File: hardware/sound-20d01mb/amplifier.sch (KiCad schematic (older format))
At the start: 0 parts

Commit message: Added TPA3122D2
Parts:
- added U?: TPA3122D2, Package_DIP:DIP-20_W7.62mm, symbol sound-20d01_Library:TPA3122D2
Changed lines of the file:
@@
 Comment4 ""
 $EndDescr
+$Comp
+L sound-20d01_Library:TPA3122D2 U?
+U 1 1 60DE3B7A
+P 5500 3500
+F 0 "U?" H 5500 4217 50  0000 C CNN
+F 1 "TPA3122D2" H 5500 4126 50  0000 C CNN
+F 2 "Package_DIP:DIP-20_W7.62mm" H 5500 2900 50  0001 C CNN
+F 3 "https://www.ti.com/lit/ds/symlink/tpa3122d2.pdf" H 5500 2800 50  0001 C CNN
+	1    5500 3500
+	1    0    0    -1
+$EndComp
 $EndSCHEMATC

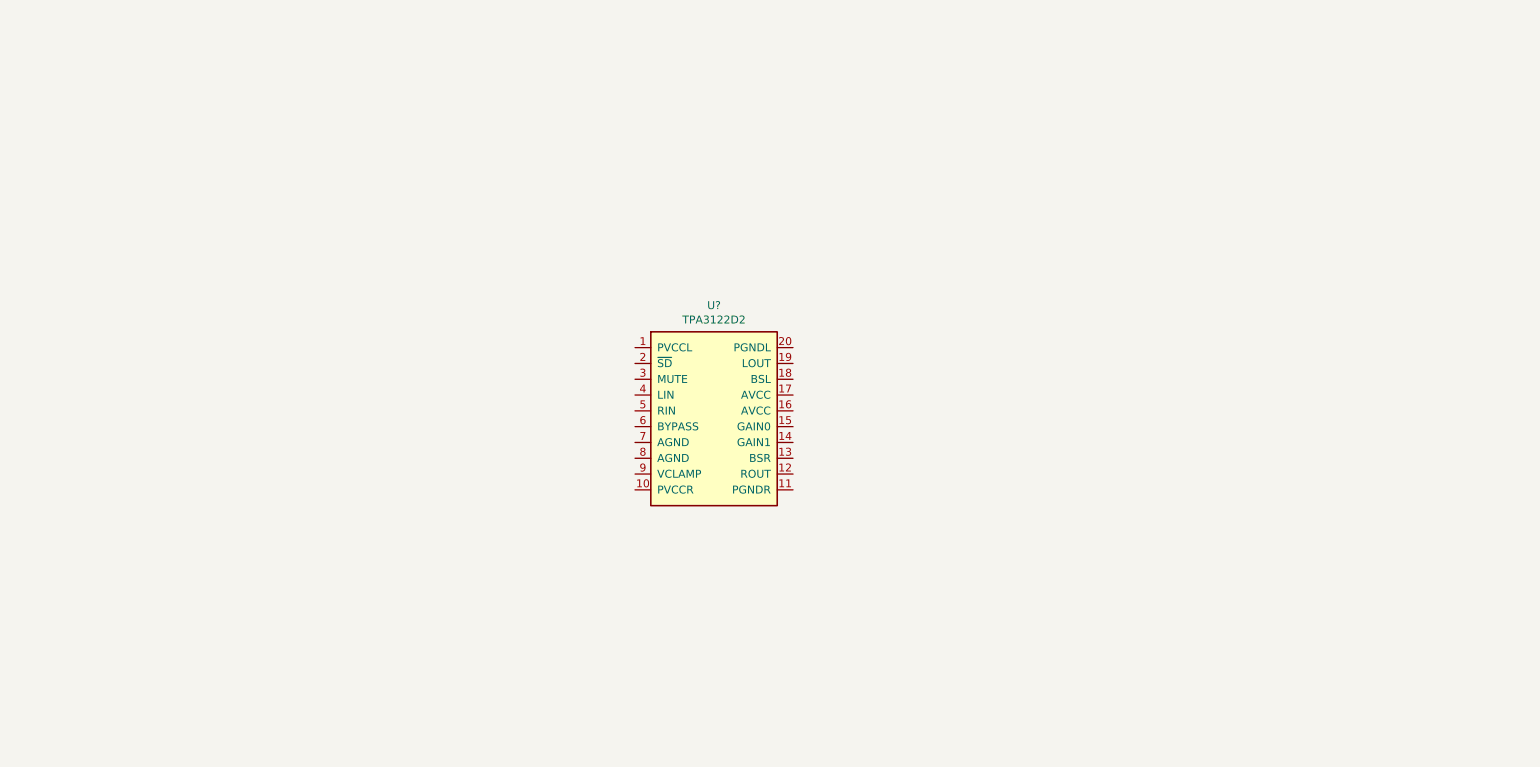
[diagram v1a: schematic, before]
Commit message: Updated amplifier schematic
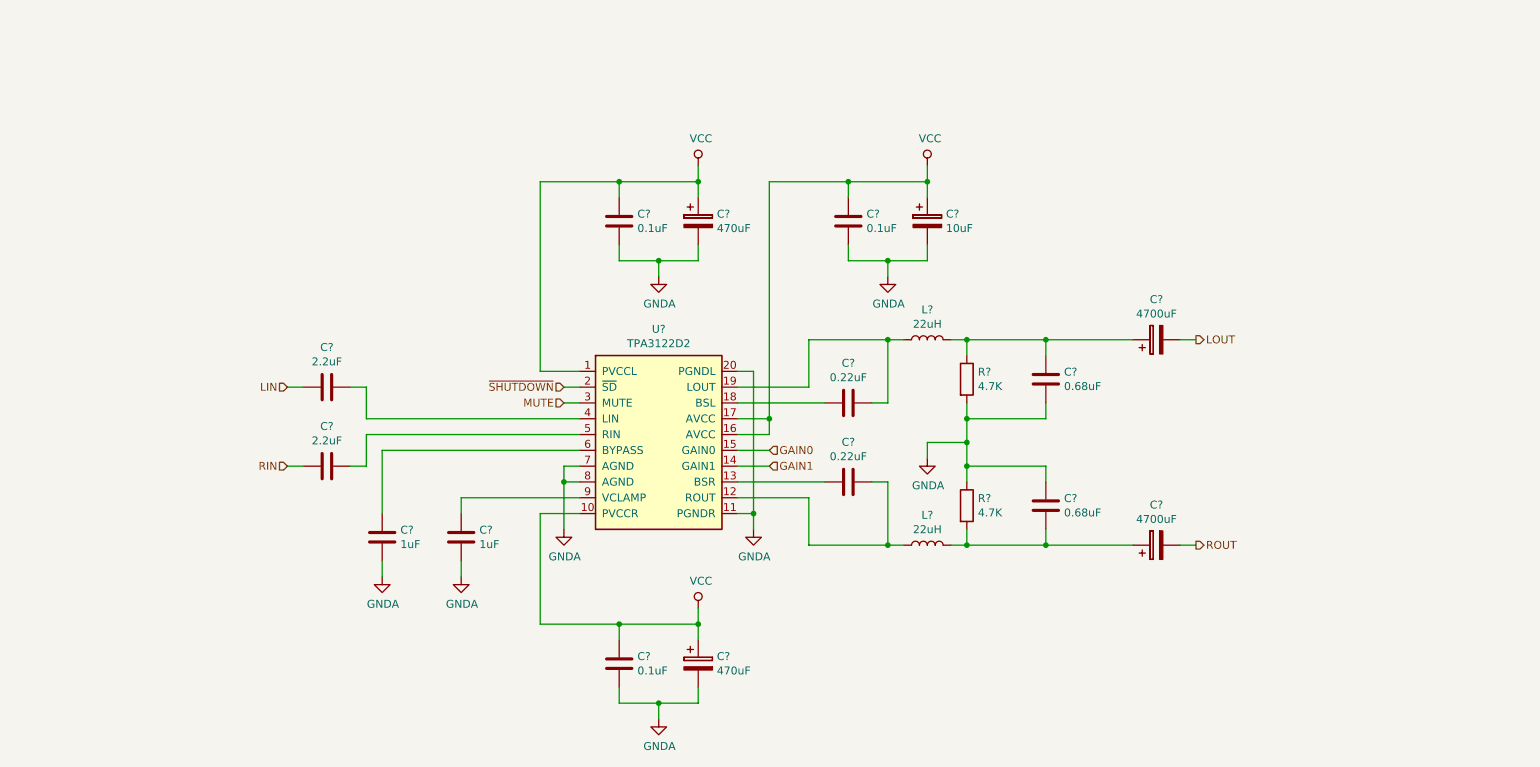
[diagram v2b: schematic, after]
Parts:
- added C? (x2): 0.22uF, Capacitor_SMD:C_1206_3216Metric_Pad1.42x1.75mm_HandSolder, symbol Device:C
- added C? (x2): 0.68uF, Capacitor_THT:C_Rect_L7.2mm_W4.5mm_P5.00mm_FKS2_FKP2_MKS2_MKP2, symbol Device:C
- added C? (x2): 4700uF, Capacitor_THT:CP_Radial_D18.0mm_P7.50mm, symbol Device:CP
- added C?: 10uF, Capacitor_THT:CP_Radial_D8.0mm_P3.50mm, symbol Device:CP
- added C? (x3): 0.1uF, Capacitor_SMD:C_1206_3216Metric_Pad1.42x1.75mm_HandSolder, symbol Device:C
- added C? (x2): 470uF, symbol Device:CP
- added C? (x2): 1uF, Capacitor_SMD:C_1206_3216Metric_Pad1.42x1.75mm_HandSolder, symbol Device:C
- added C? (x2): 2.2uF, symbol Device:C
- added L? (x2): 22uH, Inductor_SMD:L_Bourns_SRR1260, symbol Device:L
- added R? (x2): 4.7K, Resistor_SMD:R_1206_3216Metric_Pad1.42x1.75mm_HandSolder, symbol Device:R
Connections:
- net VCC: now reaches U?.1 (PVCCL)
- net VCC: now also U?.10 (PVCCR), U?.16 (AVCC), U?.17 (AVCC), C?.1, C?.1, C?.1, C?.1, C?.1, C?.1
- net GNDA: now reaches U?.11 (PGNDR)
- net GNDA: now also U?.20 (PGNDL), U?.7 (AGND), U?.8 (AGND), C?.1, C?.2, C?.2, C?.2, C?.2, C?.2, C?.2, C?.2, C?.2, C?.2, R?.1, R?.2
- net at U?.12 (ROUT): now also C?.2, L?.1
- net at U?.13 (BSR): now also C?.1
- net GAIN1: now reaches U?.14 (GAIN1)
- net GAIN0: now reaches U?.15 (GAIN0)
- net at U?.18 (BSL): now also C?.1
- net at U?.19 (LOUT): now also C?.2, L?.1
- net ~SHUTDOWN: now reaches U?.2 (~SD)
- net MUTE: now reaches U?.3 (MUTE)
- net at U?.4 (LIN): now also C?.2
- net at U?.5 (RIN): now also C?.2
- net at U?.6 (BYPASS): now also C?.1
- net at U?.9 (VCLAMP): now also C?.1
- new net: C?.1, C?.1, L?.2, R?.1
- new net: C?.1, C?.2, L?.2, R?.2
- new net LIN: C?.1
- new net LOUT: C?.2
- new net RIN: C?.1
- new net ROUT: C?.2
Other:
- moved on the sheet: U?

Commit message: Added PGA2311P
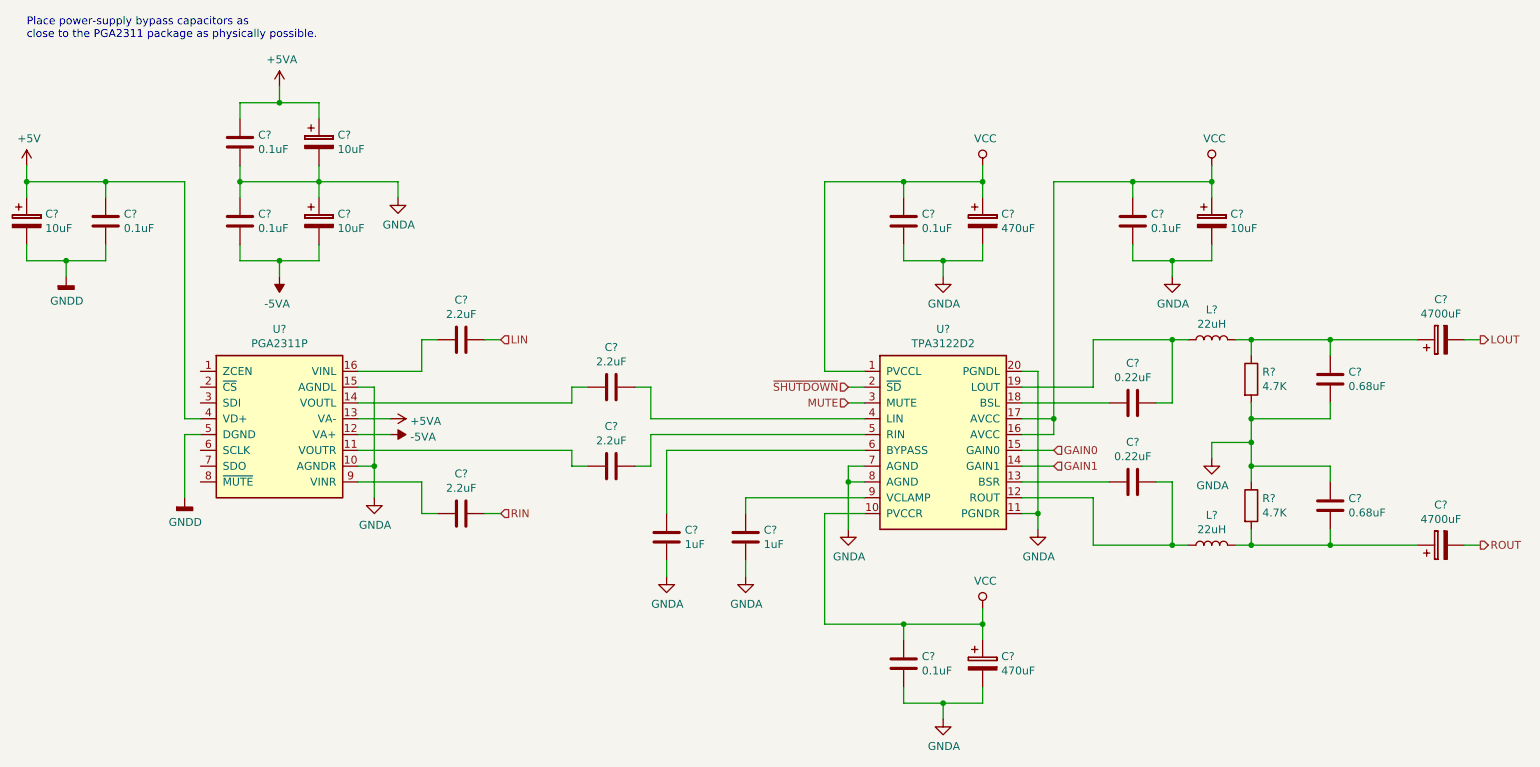
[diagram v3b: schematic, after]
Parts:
- added C? (x3): 10uF, Capacitor_THT:CP_Radial_D8.0mm_P3.50mm, symbol Device:CP
- added C? (x3): 0.1uF, Capacitor_SMD:C_1206_3216Metric_Pad1.42x1.75mm_HandSolder, symbol Device:C
- added C? (x2): 2.2uF, symbol Device:C
- added U?: PGA2311P, Package_DIP:DIP-16_W7.62mm, symbol sound-20d01_Library:PGA2311P
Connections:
- net GNDA: now also C?.1, C?.1, C?.2, C?.2, U?.10 (AGNDR), U?.15 (AGNDL)
- net LIN: now also C?.2; no longer C?.1
- net RIN: now also C?.2; no longer C?.1
- new net: C?.1, U?.11 (VOUTR)
- new net: C?.1, U?.14 (VOUTL)
- new net: C?.1, U?.16 (VINL)
- new net: C?.1, U?.9 (VINR)
- new net +5V: C?.1, C?.1, U?.4 (VD+)
- new net +5VA: C?.1, C?.1, U?.13 (VA-)
- new net -5VA: C?.2, C?.2, U?.12 (VA+)
- new net GNDD: C?.2, C?.2, U?.5 (DGND)
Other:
- note added: "Place power-supply bypass capacitors as\nclose to the PGA2311 package as physically possible."
- moved on the sheet: C?, L?, R?, U?
